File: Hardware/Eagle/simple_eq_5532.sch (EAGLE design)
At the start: 40 parts, among them IC1 NE5532, IC2 NE5532

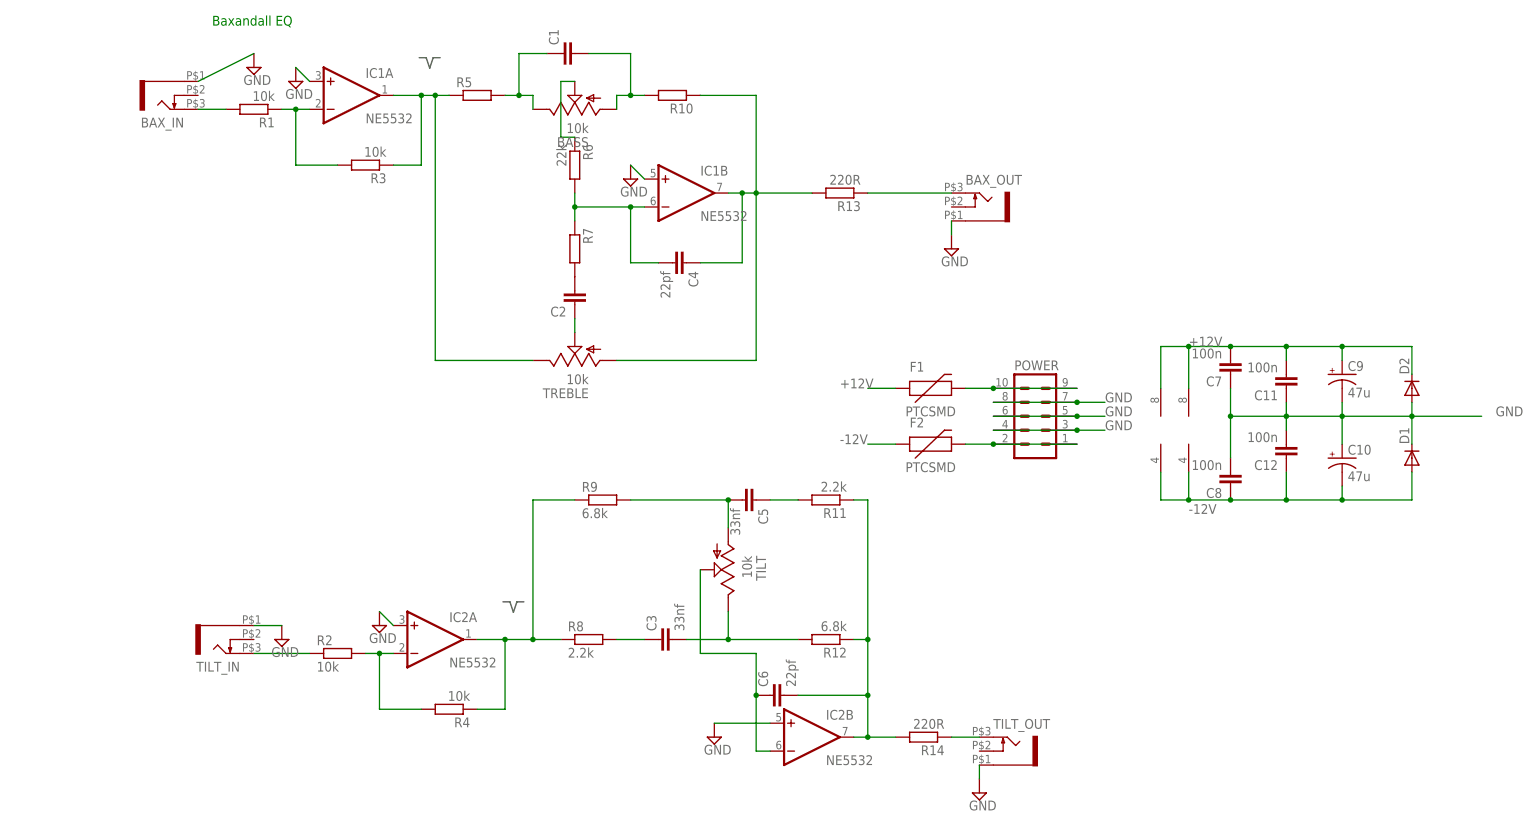
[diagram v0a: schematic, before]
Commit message: Rev 1.1 updated Thonkiconn socket outlines
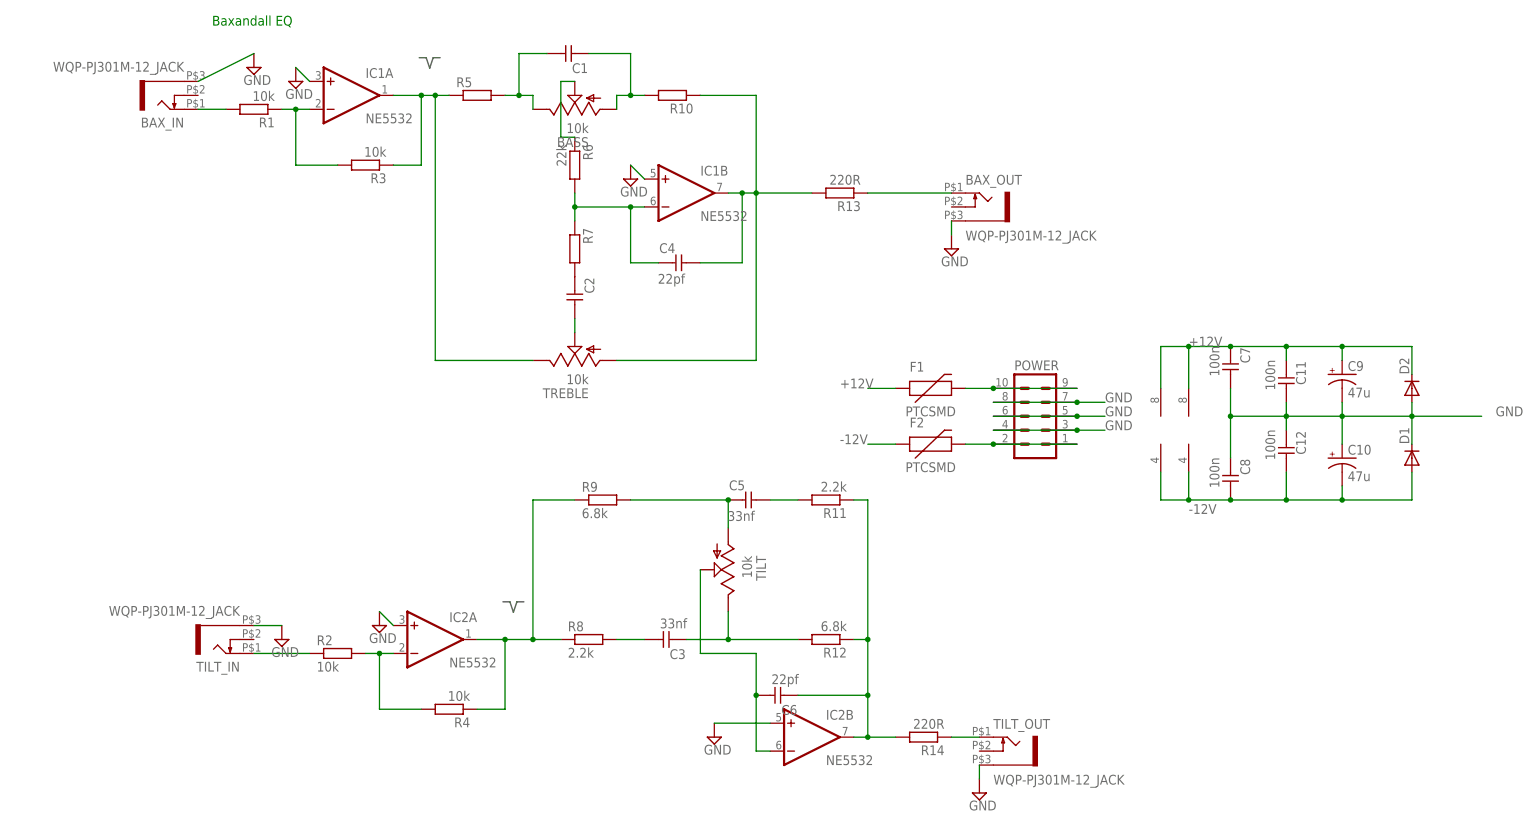
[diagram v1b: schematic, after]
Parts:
- BAX_IN, BAX_OUT, TILT_IN, TILT_OUT: value THONKICONN -> WQP-PJ301M-12_JACK; device TomW:THONKICONN -> thonkiconn:WQP-PJ301M-12_JACK
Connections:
- net BAX$1: now also BAX_IN.2; no longer BAX_IN.3
- net BAX$2: now also BAX_OUT.2; no longer BAX_OUT.3
- net GND: now also BAX_IN.1, BAX_OUT.1, TILT_IN.1, TILT_OUT.1; no longer BAX_IN.5, BAX_OUT.5, TILT_IN.5, TILT_OUT.5
- net N$5: now also TILT_OUT.2; no longer TILT_OUT.3
- net N$6: now also TILT_IN.2; no longer TILT_IN.3
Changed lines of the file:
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@@
 <?xml version="1.0" encoding="utf-8"?>
 <!DOCTYPE eagle SYSTEM "eagle.dtd">
-<eagle version="6.5.0">
+<eagle version="6.6.0">
 <drawing>
 <settings>
@@
 <layer number="54" name="bGND_GNDA" color="1" fill="9" visible="no" active="no"/>
 <layer number="56" name="wert" color="7" fill="1" visible="no" active="no"/>
+<layer number="57" name="tCAD" color="7" fill="1" visible="no" active="no"/>
 <layer number="91" name="Nets" color="2" fill="1" visible="yes" active="yes"/>
 <layer number="92" name="Busses" color="1" fill="1" visible="yes" active="yes"/>
@@
 <layer number="108" name="tplace-old" color="10" fill="1" visible="yes" active="yes"/>
 <layer number="109" name="ref-old" color="11" fill="1" visible="yes" active="yes"/>
+<layer number="110" name="110" color="7" fill="1" visible="no" active="no"/>
+<layer number="111" name="111" color="7" fill="1" visible="no" active="no"/>
+<layer number="112" name="tSilk" color="7" fill="1" visible="no" active="no"/>
 <layer number="116" name="Patch_BOT" color="9" fill="4" visible="no" active="yes"/>
+<layer number="118" name="Rect_Pads" color="7" fill="1" visible="no" active="no"/>
 <layer number="121" name="_tsilk" color="7" fill="1" visible="no" active="yes"/>
 <layer number="122" name="_bsilk" color="7" fill="1" visible="no" active="yes"/>
+<layer number="123" name="tTestmark" color="7" fill="1" visible="no" active="no"/>
+<layer number="124" name="bTestmark" color="7" fill="1" visible="no" active="no"/>
 <layer number="125" name="_tNames" color="7" fill="1" visible="no" active="yes"/>
+<layer number="126" name="_bNames" color="7" fill="1" visible="no" active="no"/>
+<layer number="127" name="_tValues" color="7" fill="1" visible="no" active="no"/>
+<layer number="128" name="_bValues" color="7" fill="1" visible="no" active="no"/>
+<layer number="131" name="prix" color="7" fill="1" visible="yes" active="yes"/>
+<layer number="132" name="test" color="7" fill="1" visible="yes" active="yes"/>
 <layer number="144" name="Drill_legend" color="7" fill="1" visible="no" active="yes"/>
+<layer number="150" name="Notes" color="7" fill="1" visible="yes" active="yes"/>
 <layer number="151" name="HeatSink" color="7" fill="1" visible="no" active="yes"/>
+<layer number="152" name="_bDocu" color="7" fill="1" visible="no" active="no"/>
+<layer number="153" name="FabDoc1" color="6" fill="1" visible="no" active="no"/>
+<layer number="154" name="FabDoc2" color="2" fill="1" visible="no" active="no"/>
+<layer number="155" name="FabDoc3" color="7" fill="15" visible="no" active="no"/>
 <layer number="199" name="Contour" color="7" fill="1" visible="yes" active="yes"/>
 <layer number="200" name="200bmp" color="1" fill="10" visible="yes" active="yes"/>
@@
 <layer number="223" name="223bmp" color="24" fill="1" visible="no" active="no"/>
 <layer number="224" name="224bmp" color="25" fill="1" visible="no" active="no"/>
+<layer number="248" name="Housing" color="7" fill="1" visible="no" active="no"/>
+<layer number="249" name="Edge" color="7" fill="1" visible="no" active="no"/>
 <layer number="250" name="Descript" color="3" fill="1" visible="no" active="no"/>
 <layer number="251" name="SMDround" color="12" fill="11" visible="no" active="no"/>
@@
 <part name="R7" library="TomW" deviceset="R-EU_" device="R0805"/>
 <part name="C4" library="TomW" deviceset="C-EU" device="0805_CAP" value="22pf"/>
-<part name="BAX_IN" library="TomW" deviceset="THONKICONN" device="" value=""/>
+<part name="BAX_IN" library="thonkiconn" deviceset="WQP-PJ301M-12_JACK" device="" value="WQP-PJ301M-12_JACK"/>
 <part name="SUPPLY1" library="supply2" deviceset="GND" device=""/>
 <part name="R13" library="TomW" deviceset="R-EU_" device="R0805" value="220R"/>
-<part name="BAX_OUT" library="TomW" deviceset="THONKICONN" device="" value=""/>
+<part name="BAX_OUT" library="thonkiconn" deviceset="WQP-PJ301M-12_JACK" device="" value="WQP-PJ301M-12_JACK"/>
 <part name="SUPPLY2" library="supply2" deviceset="GND" device=""/>
 <part name="R2" library="TomW" deviceset="R-EU_" device="R0805" value="10k"/>
@@
 <part name="SUPPLY12" library="supply2" deviceset="GND" device=""/>
 <part name="C6" library="TomW" deviceset="C-EU" device="0805_CAP" value="22pf"/>
-<part name="TILT_IN" library="TomW" deviceset="THONKICONN" device="" value=""/>
+<part name="TILT_IN" library="thonkiconn" deviceset="WQP-PJ301M-12_JACK" device="" value="WQP-PJ301M-12_JACK"/>
 <part name="R14" library="TomW" deviceset="R-EU_" device="R0805" value="220R"/>
-<part name="TILT_OUT" library="TomW" deviceset="THONKICONN" device="" value=""/>
+<part name="TILT_OUT" library="thonkiconn" deviceset="WQP-PJ301M-12_JACK" device="" value="WQP-PJ301M-12_JACK"/>
 <part name="SUPPLY4" library="supply2" deviceset="GND" device=""/>
 <part name="SUPPLY5" library="supply2" deviceset="GND" device=""/>
@@
 </segment>
 <segment>
-<pinref part="BAX_IN" gate="G$1" pin="5"/>
+<pinref part="BAX_IN" gate="G$1" pin="1"/>
 <pinref part="SUPPLY1" gate="GND" pin="GND"/>
 <wire x1="48.26" y1="142.24" x2="38.1" y2="137.16" width="0.1524" layer="91"/>
 </segment>
 <segment>
-<pinref part="BAX_OUT" gate="G$1" pin="5"/>
+<pinref part="BAX_OUT" gate="G$1" pin="1"/>
 <pinref part="SUPPLY2" gate="GND" pin="GND"/>
 <wire x1="175.26" y1="109.22" x2="175.26" y2="111.76" width="0.1524" layer="91"/>
@@
 </segment>
 <segment>
-<pinref part="TILT_OUT" gate="G$1" pin="5"/>
+<pinref part="TILT_OUT" gate="G$1" pin="1"/>
 <pinref part="SUPPLY4" gate="GND" pin="GND"/>
 <wire x1="180.34" y1="10.16" x2="180.34" y2="12.7" width="0.1524" layer="91"/>
 </segment>
 <segment>
-<pinref part="TILT_IN" gate="G$1" pin="5"/>
+<pinref part="TILT_IN" gate="G$1" pin="1"/>
 <pinref part="SUPPLY5" gate="GND" pin="GND"/>
 <wire x1="53.34" y1="38.1" x2="48.26" y2="38.1" width="0.1524" layer="91"/>
@@
 <segment>
 <pinref part="R1" gate="G$1" pin="2"/>
-<pinref part="BAX_IN" gate="G$1" pin="3"/>
+<pinref part="BAX_IN" gate="G$1" pin="2"/>
 <wire x1="38.1" y1="132.08" x2="43.18" y2="132.08" width="0.1524" layer="91"/>
 </segment>
@@
 <segment>
 <pinref part="R13" gate="G$1" pin="1"/>
-<pinref part="BAX_OUT" gate="G$1" pin="3"/>
+<pinref part="BAX_OUT" gate="G$1" pin="2"/>
 <wire x1="175.26" y1="116.84" x2="160.02" y2="116.84" width="0.1524" layer="91"/>
 </segment>
@@
 <segment>
 <pinref part="R14" gate="G$1" pin="1"/>
-<pinref part="TILT_OUT" gate="G$1" pin="3"/>
+<pinref part="TILT_OUT" gate="G$1" pin="2"/>
 <wire x1="180.34" y1="17.78" x2="175.26" y2="17.78" width="0.1524" layer="91"/>
 </segment>
@@
 <segment>
 <pinref part="R2" gate="G$1" pin="1"/>
-<pinref part="TILT_IN" gate="G$1" pin="3"/>
+<pinref part="TILT_IN" gate="G$1" pin="2"/>
 <wire x1="48.26" y1="33.02" x2="58.42" y2="33.02" width="0.1524" layer="91"/>
 </segment>
